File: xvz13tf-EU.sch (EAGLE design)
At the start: 8 parts

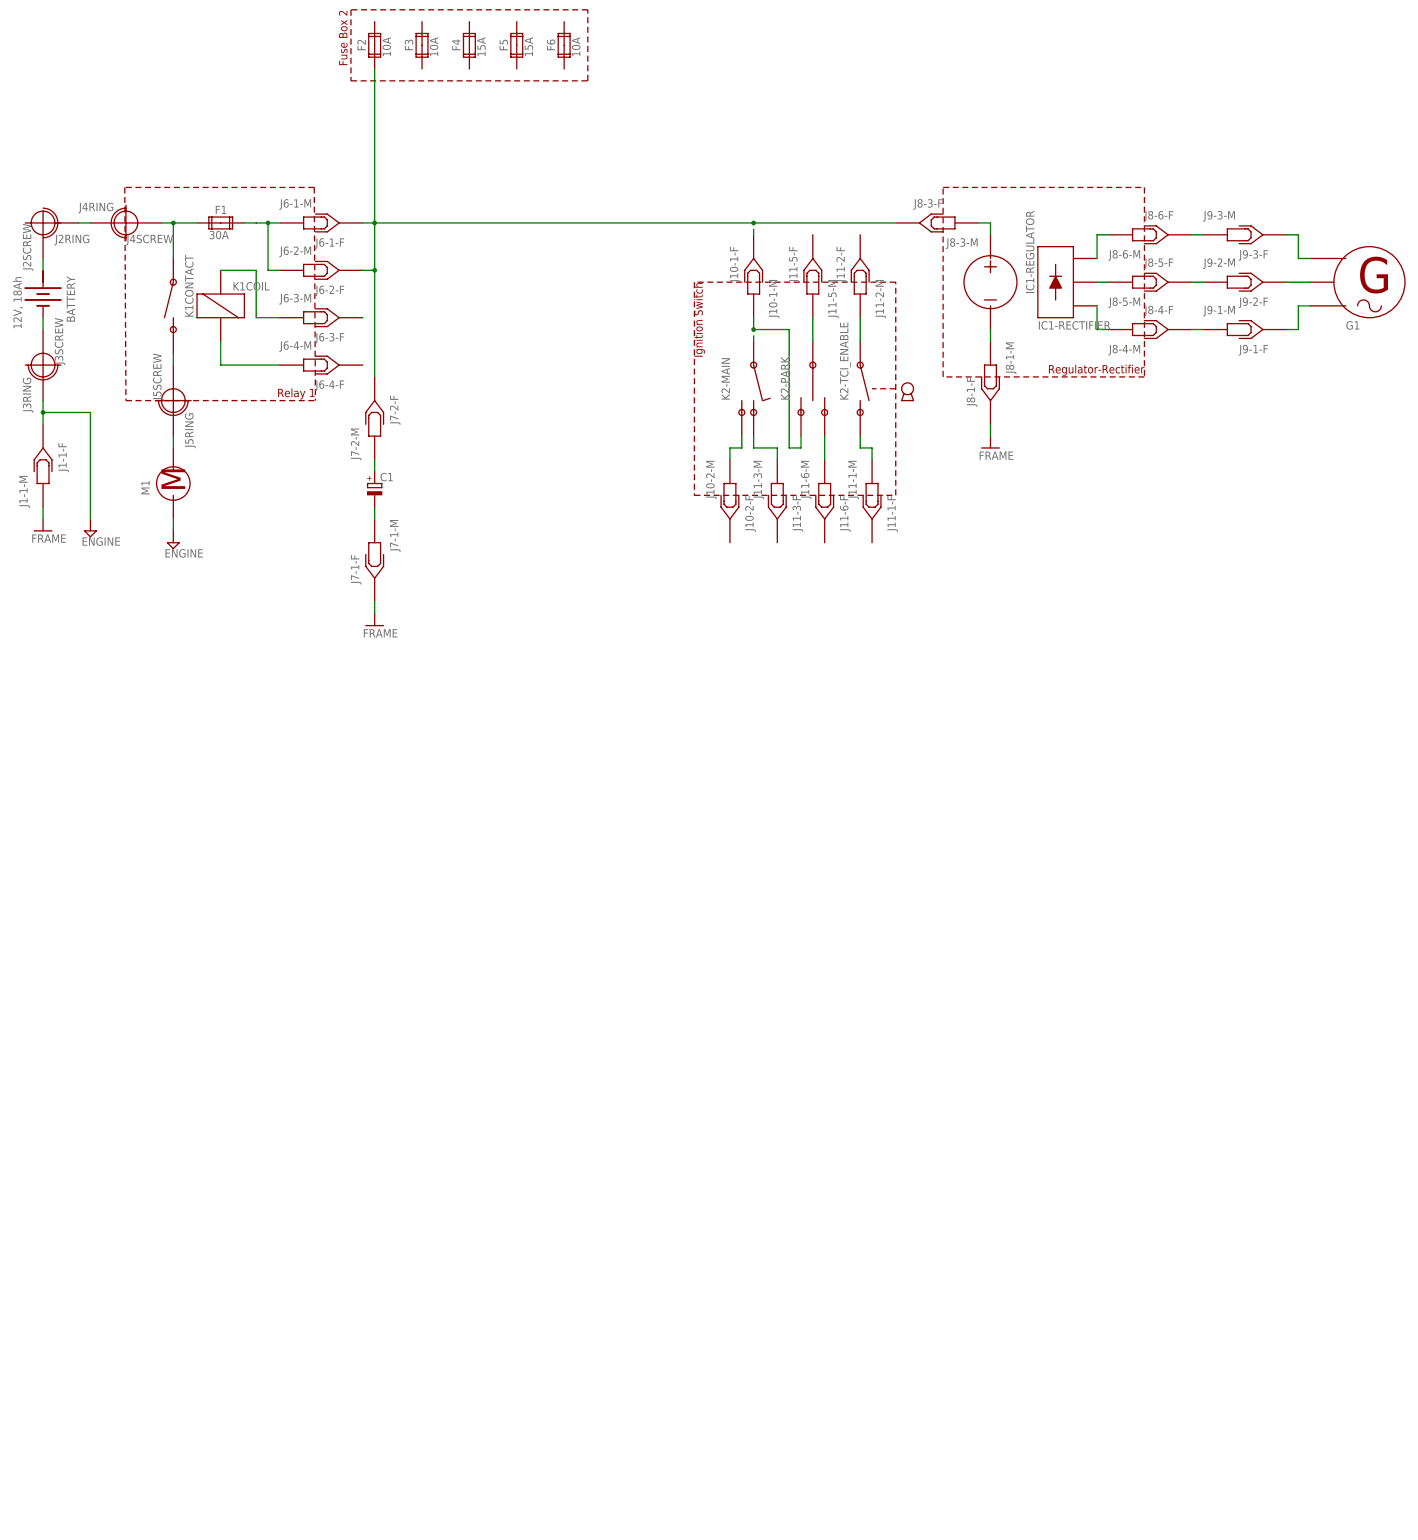
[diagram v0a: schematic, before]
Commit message: Carb heater and radiator fan circuits added  - added heater symbol to the library  - added thermo-switch symbol to the library  - complete carb heater circuit done  - complete radiator fan circuit done
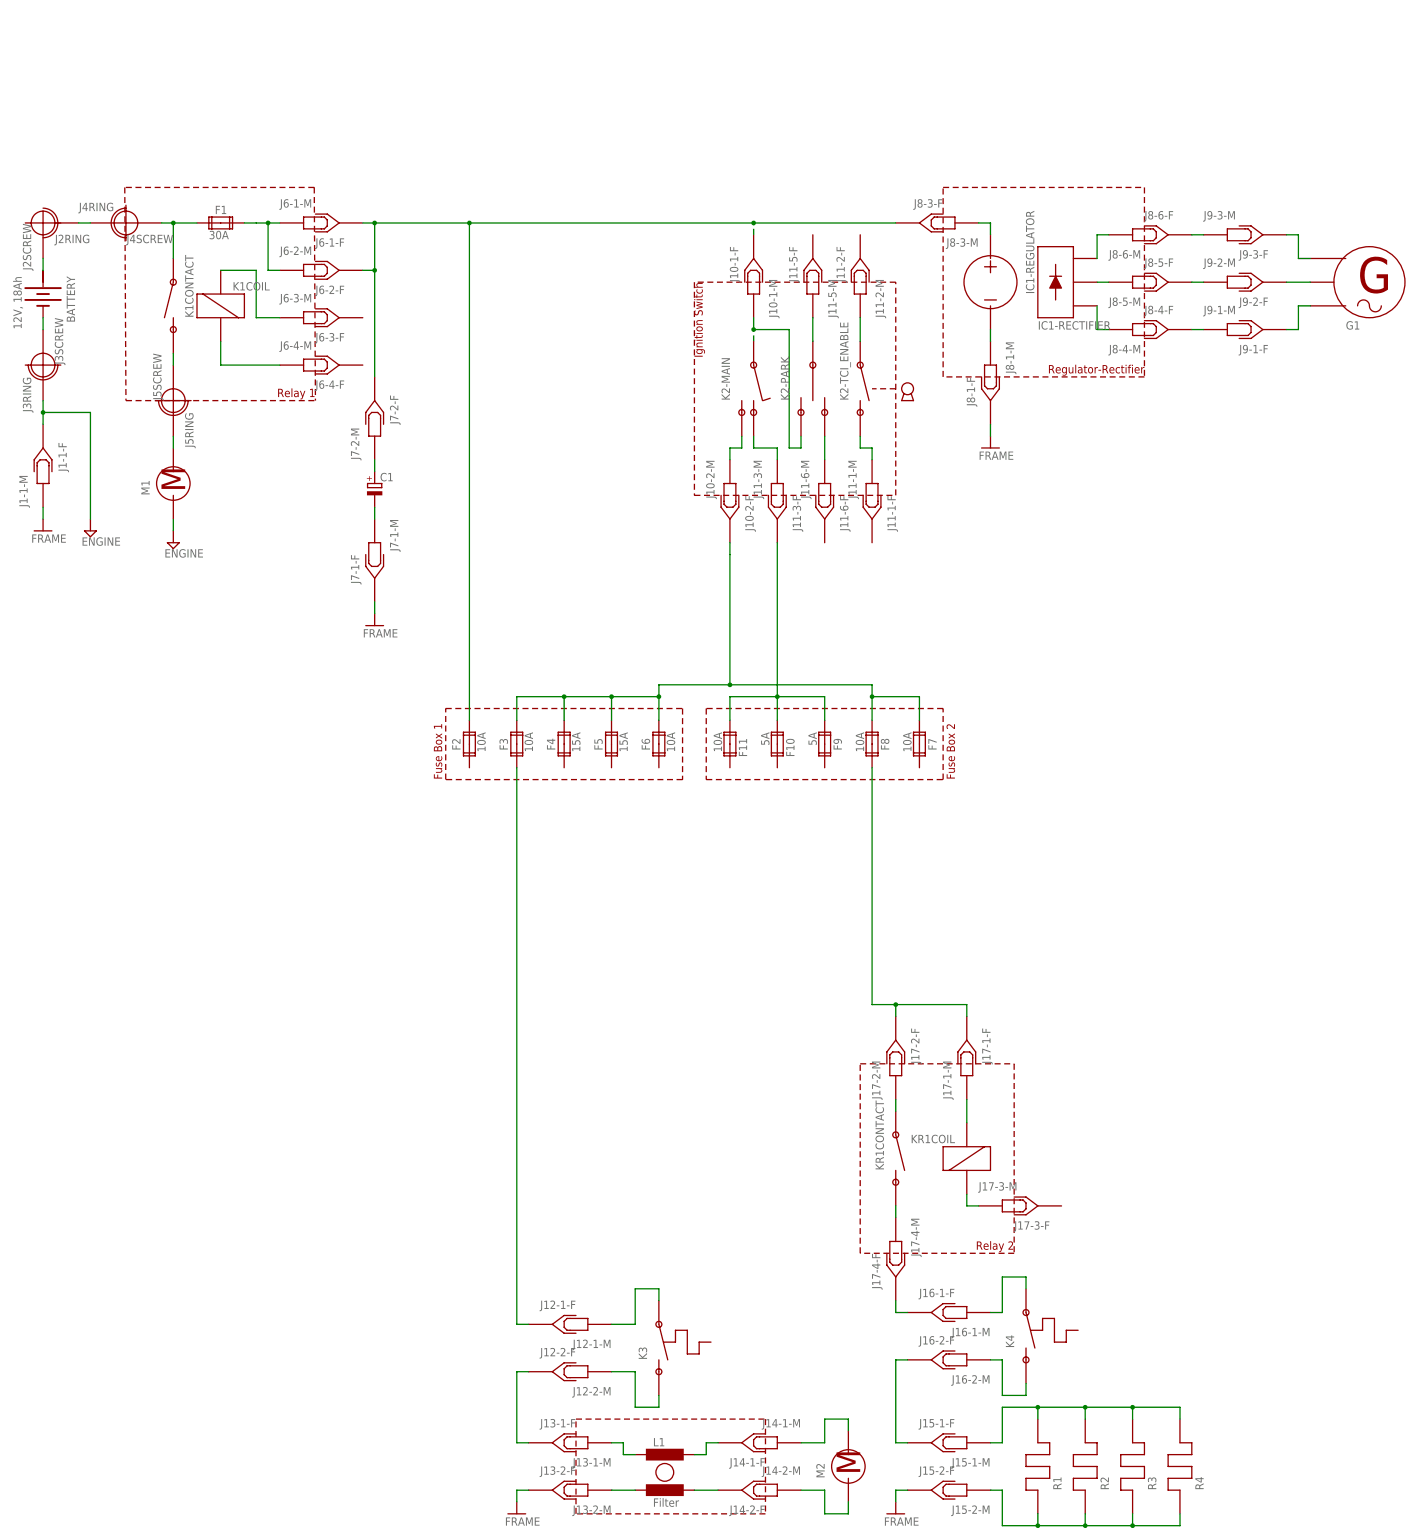
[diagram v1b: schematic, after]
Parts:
- added F10, F9: 5A, special:FUSE2P
- added F11, F7, F8: 10A, special:FUSE2P
- added L1: Filter, inductor-neosid:R18
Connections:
- net P$1: now also F10.1A, F11.1A, F3.1A, F3.2A, F4.1A, F5.1A, F6.1A, F7.1A, F8.1A, F8.2A, F9.1A, L1.1, L1.2, L1.3, L1.4
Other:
- note added: "Fuse Box 1"
- note added: "Relay 2"
- moved on the sheet: F2, F3, F4, F5, F6
